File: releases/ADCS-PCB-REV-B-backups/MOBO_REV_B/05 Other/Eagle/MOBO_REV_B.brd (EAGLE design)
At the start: 91 x 91 mm, 139 parts, among them J1 HDR_10_EZFET_DEBUGGER, J3 832-10-012-10-005000, J5 CNC_3221-10-0300-00, J7 830-10-003-20-005000, J8 830-10-006-20-005000, Q1 BSR802NL6327HTSA1, U1 MSP430F5529IPN, U10 TSV991AILT, U2 TSV991AILT, U3 ADS7841E_2K5, U4 TSV991AILT, U5 DMC4050SSDQ-13, U6 BNO055, U7 HMC1053, U9 BMX160, Y1 32.768kHz, Y2 CSTCR4M00G15L99, Y3 32.768kHz

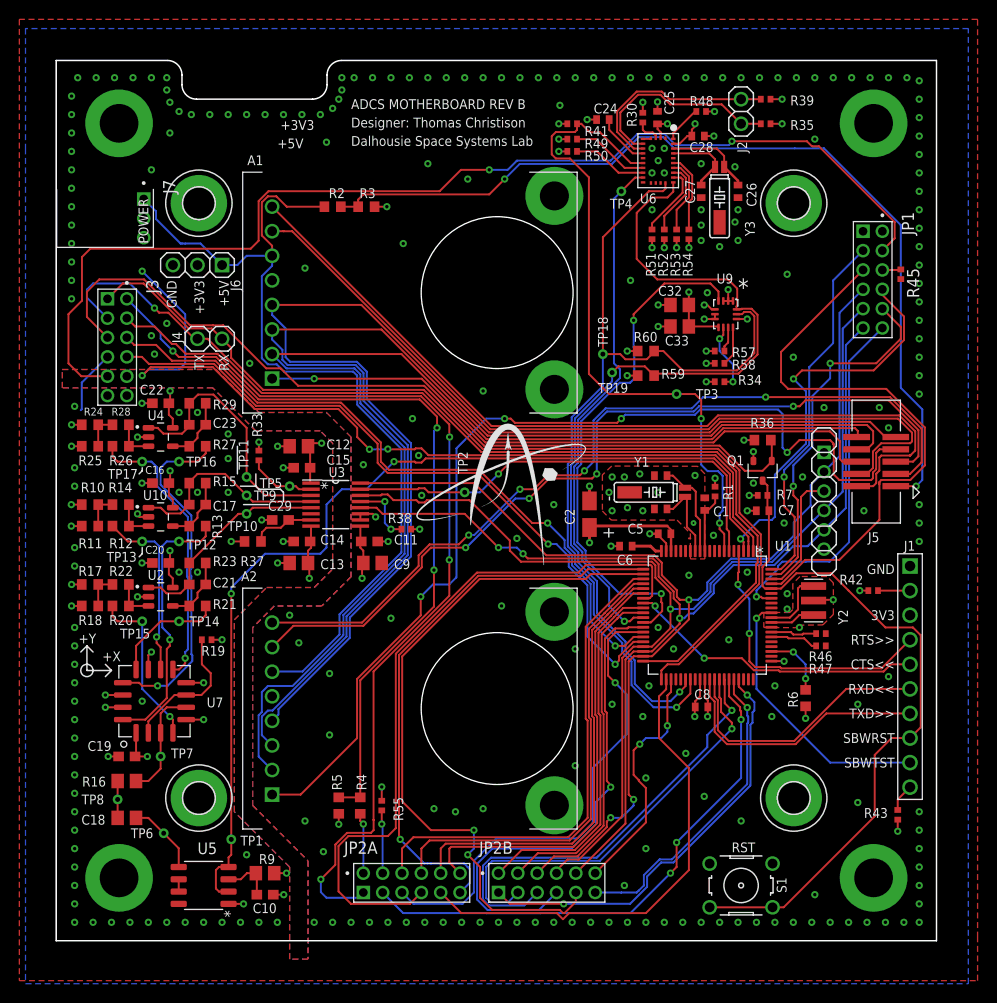
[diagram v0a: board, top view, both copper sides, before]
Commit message: Finalized connectors for Luc and reattached burn wire
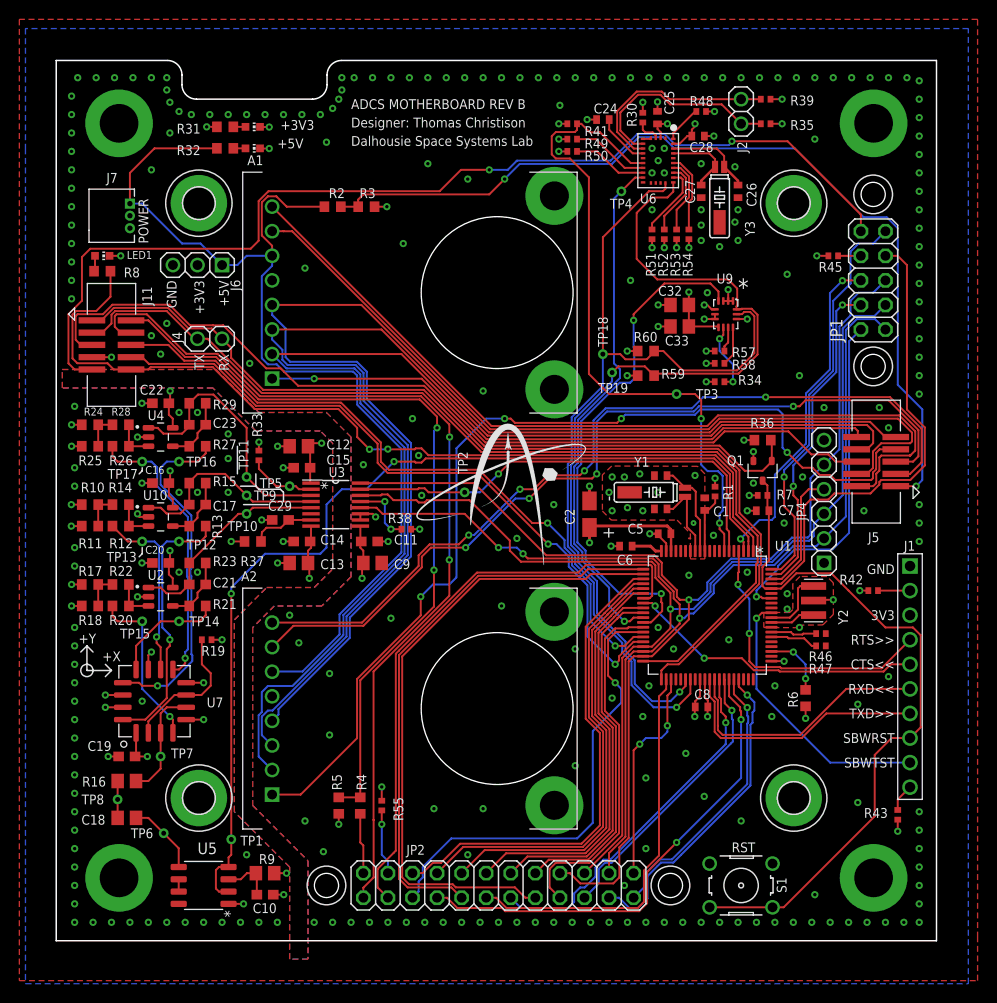
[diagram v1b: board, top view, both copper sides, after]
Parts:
- removed J3, JP2A, JP2B: 832-10-012-10-005000, 832-10-012-10-005000:832-10-012-10-005000
- removed J8: 830-10-006-20-005000, 830-10-006-20-005000:830-10-006-20-005000
- added J11: CNC_3221-10-0300-00, my_library:CNC_3221-10-0300-00
- added JP2: (no value), pinhead:2X12
- added JP4: (no value), my_library:1X06
- added LED1, LED2, LED3: (no value), led:CHIP-LED0603
- added R31, R8: 470R, rcl:R0603
- added R32: 750R, rcl:R0603
- J7: value 830-10-003-20-005000 -> TE-1734829-3; device 830-10-003-20-005000:830-10-003-20-005000 -> my_library:TE-1734829-3
- JP1: value 832-10-012-10-005000 -> (none); device 832-10-012-10-005000:832-10-012-10-005000 -> pinhead:2X05
- moved R45 7.24 mm to (80.3, 70.8), turned to 180 degrees
- moved JP1 5.17 mm to (84.5, 68.3), turned to 90 degrees
- moved J7 1.51 mm to (7.62, 76.2), turned to 90 degrees
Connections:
- new net N$4: LED1.A, R8.2
- new net N$5: LED2.A, R31.2
- new net N$6: LED3.A, R32.2
- net !CS!_CURR_SENSE_MTQR: now also JP2.23; no longer JP2B.11
- net !CS!_CURR_SENSE_RW: now also JP2.21; no longer JP2B.1
- net !CS!_SPD_SENSE_RW: now also JP2.24; no longer JP2B.12
- net !CS!_SUN_X+: now also JP1.2; no longer JP1.12
- net !CS!_SUN_X-: now also JP1.7; no longer JP1.5
- net !CS!_SUN_Y+: now also JP1.4; no longer JP1.10
- net !CS!_SUN_Y-: now also JP1.9; no longer JP1.3
- net !CS!_SUN_Z+: now also JP4.4; no longer J8.3
- net !CS!_SUN_Z-: now also JP1.6; no longer JP1.8
- net +3V3: now also J11.7, JP4.1, R31.1; no longer J3.7, J8.6
- net +5V: now also R32.1
- net ACT_BRD_3V_PRESENT: now also J11.4, JP2.1; no longer J3.4, JP2A.1
- net ACT_BRD_5V_PRESENT: now also JP2.2; no longer JP2A.2
- net ACT_BRD_5V_SHIFTED: now also J11.2; no longer J3.2
- net GND: now also JP4.6, LED1.C, LED2.C, LED3.C; no longer J8.1
- net MAG_X_FIN: now also JP2.8; no longer JP2A.8
- net MAG_X_RIN: now also JP2.6; no longer JP2A.6
- net MAG_Y_FIN: now also JP2.12; no longer JP2A.12
- net MAG_Y_RIN: now also JP2.10; no longer JP2A.10
- net MAG_Z_FIN: now also JP2.16; no longer JP2B.4
- net MAG_Z_RIN: now also JP2.14; no longer JP2B.2
- net MSP430_ACTIVE: now also J11.10, R8.1
- net MSP_OBC_RESET: now also J11.5; no longer J3.5
- net N$1: now also JP2.4; no longer JP2A.4
- net N$58: now also JP1.8; no longer JP1.6
- net RESERVED_1: now also J11.6; no longer J3.6
- net RESERVED_2: now also J11.8; no longer J3.8
- net RW_X_DIR: now also JP2.13; no longer JP2B.3
- net RW_X_LOCK: now also JP2.9; no longer JP2A.11
- net RW_X_SPEED_CTRL: now also JP2.11; no longer JP2A.9
- net RW_Y_DIR: now also JP2.19; no longer JP2B.5
- net RW_Y_LOCK: now also JP2.15; no longer JP2B.9
- net RW_Y_SPEED_CTRL: now also JP2.17; no longer JP2B.7
- net RW_Z_DIR: now also JP2.7; no longer JP2A.3
- net RW_Z_LOCK: now also JP2.3; no longer JP2A.7
- net RW_Z_SPEED_CTRL: now also JP2.5; no longer JP2A.5
- net UCA0RXD: now also J11.1; no longer J3.1
- net UCA0TXD: now also J11.3; no longer J3.3
- net UCB0_SPI_CLK: now also JP1.5, JP2.18, JP4.5; no longer J8.2, JP1.7, JP2B.6
- net UCB0_SPI_MISO: now also JP1.1, JP2.22, JP4.2; no longer J8.5, JP1.11, JP2B.10
- net UCB0_SPI_MOSI: now also JP1.3, JP2.20, JP4.3; no longer J8.4, JP1.9, JP2B.8
- net Z-_SUN_3V_PRESENT: now also J11.9, JP1.10; no longer J3.9, JP1.4
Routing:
- net RW_Y_DIR: track 46.5 -> 29.7 mm
- net RW_Y_SPEED_CTRL: track 51.6 -> 37.3 mm, vias 1 -> 0
- net +5V: track 91.6 -> 105.6 mm
- net RW_Z_LOCK: track 73.4 -> 60.9 mm
- net !CS!_CURR_SENSE_RW: track 44.0 -> 33.5 mm, vias 2 -> 1
- net !CS!_SUN_X-: track 59.0 -> 48.5 mm
- net RW_X_SPEED_CTRL: track 50.2 -> 41.0 mm
- net Z-_SUN_3V_PRESENT: track 115.5 -> 108.0 mm
- net RW_X_DIR: track 44.0 -> 37.7 mm
- net !CS!_SUN_Z-: track 41.3 -> 35.1 mm
- net RW_Y_LOCK: track 71.9 -> 66.2 mm, vias 2 -> 0
- net RW_Z_DIR: track 55.9 -> 50.3 mm, vias 3 -> 2
- net UCB0_SPI_CLK: track 121.0 -> 126.0 mm, vias 3 -> 1
- net UCA0TXD: track 106.8 -> 102.4 mm, vias 1 -> 0
- net GND: track 80.4 -> 84.7 mm, vias 313 -> 317
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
